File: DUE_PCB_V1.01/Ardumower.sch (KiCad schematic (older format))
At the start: 54 parts, among them J1 I2C0_1, J10 Bumper Left, J11 Bumper Right, J12 P_Left, J13 P_Right, J14 Sonar_R, J15 Sonar_C, J16 Sonar_L, J17 US1, J18 US2, J19 US3, J2 I2C0_2, J20 Button, J21 5V IN, J22 Remote, J23 PCB_2, J24 3.3V IN, J25 Ser0, J26 Ser1, J27 Ser2 (ESP32), J28 GPS_TX/GPS_RX, J3 I2C1_1, J5 9V IN, J6 Drop_Left, J7 Drop_Right, J8 Tilt, J9 Rain

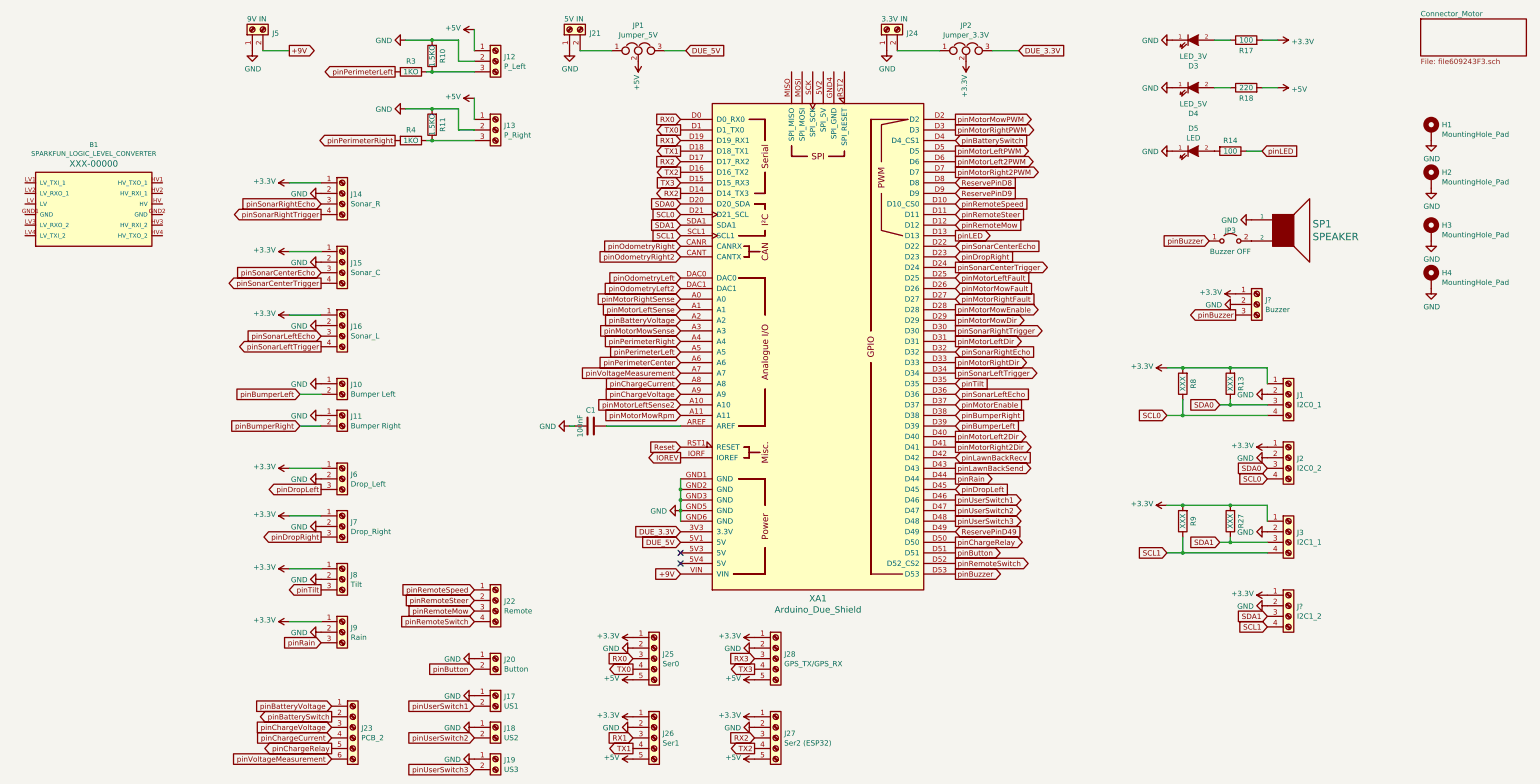
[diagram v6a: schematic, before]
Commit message: Add Reserve Pin Connectors
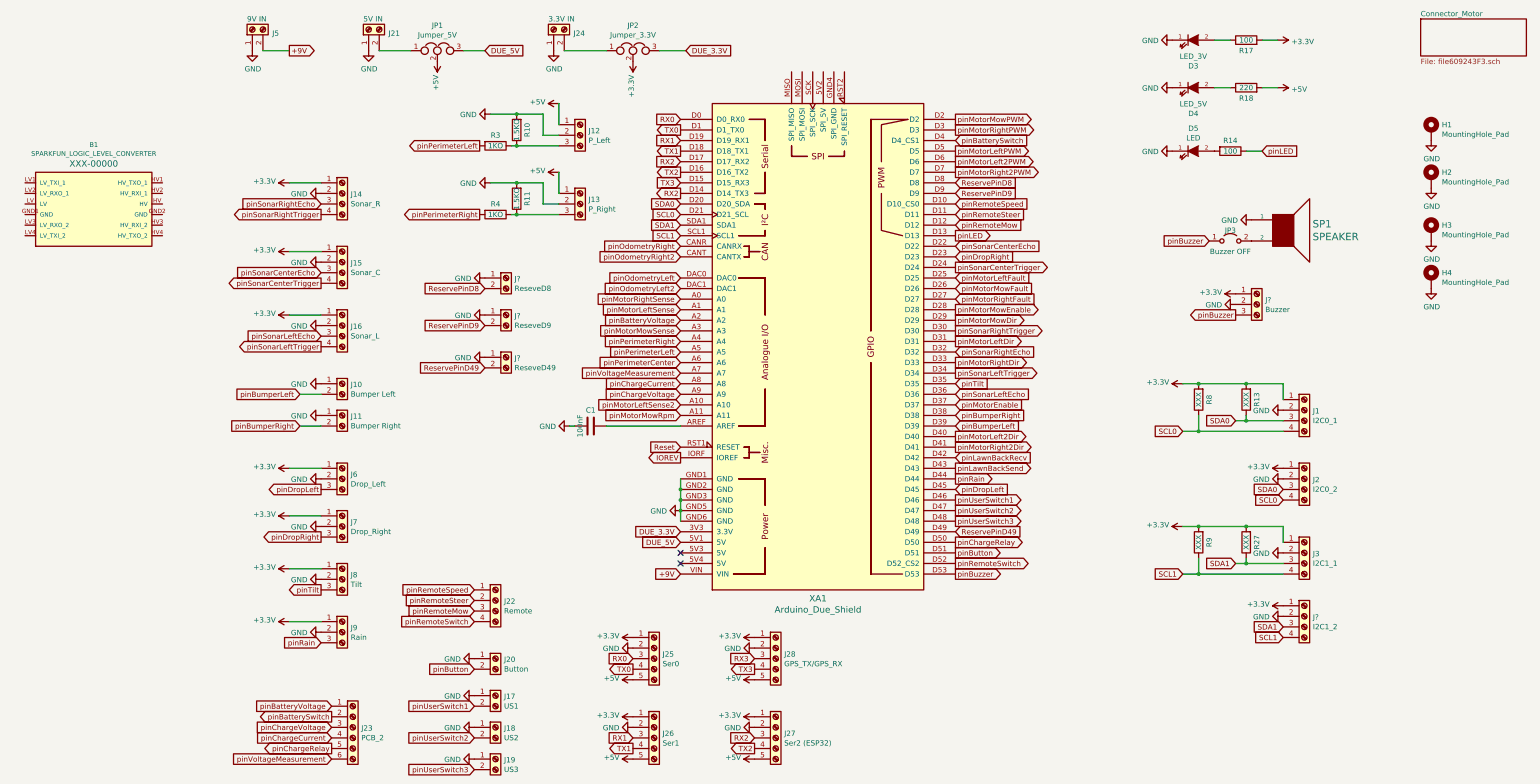
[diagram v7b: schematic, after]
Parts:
- added J?: ReseveD8, Zimprich:Pin_Header_KK110_1x02_3D, symbol Connector:Screw_Terminal_01x02
- added J?: ReseveD9, Zimprich:Pin_Header_KK110_1x02_3D, symbol Connector:Screw_Terminal_01x02
- added J?: ReseveD49, Zimprich:Pin_Header_KK110_1x02_3D, symbol Connector:Screw_Terminal_01x02
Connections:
- net GND: now also J?.1 (Pin_1), J?.1 (Pin_1), J?.1 (Pin_1)
- net ReservePinD49: now also J?.2 (Pin_2)
- net ReservePinD8: now also J?.2 (Pin_2)
- net ReservePinD9: now also J?.2 (Pin_2)
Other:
- moved on the sheet: J1, J12, J13, J2, J21, J24, J3, J?, JP1, JP2, R10, R11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

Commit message: Change Pin Header to JST
Change Pin Header to JST and sort them on the PCB
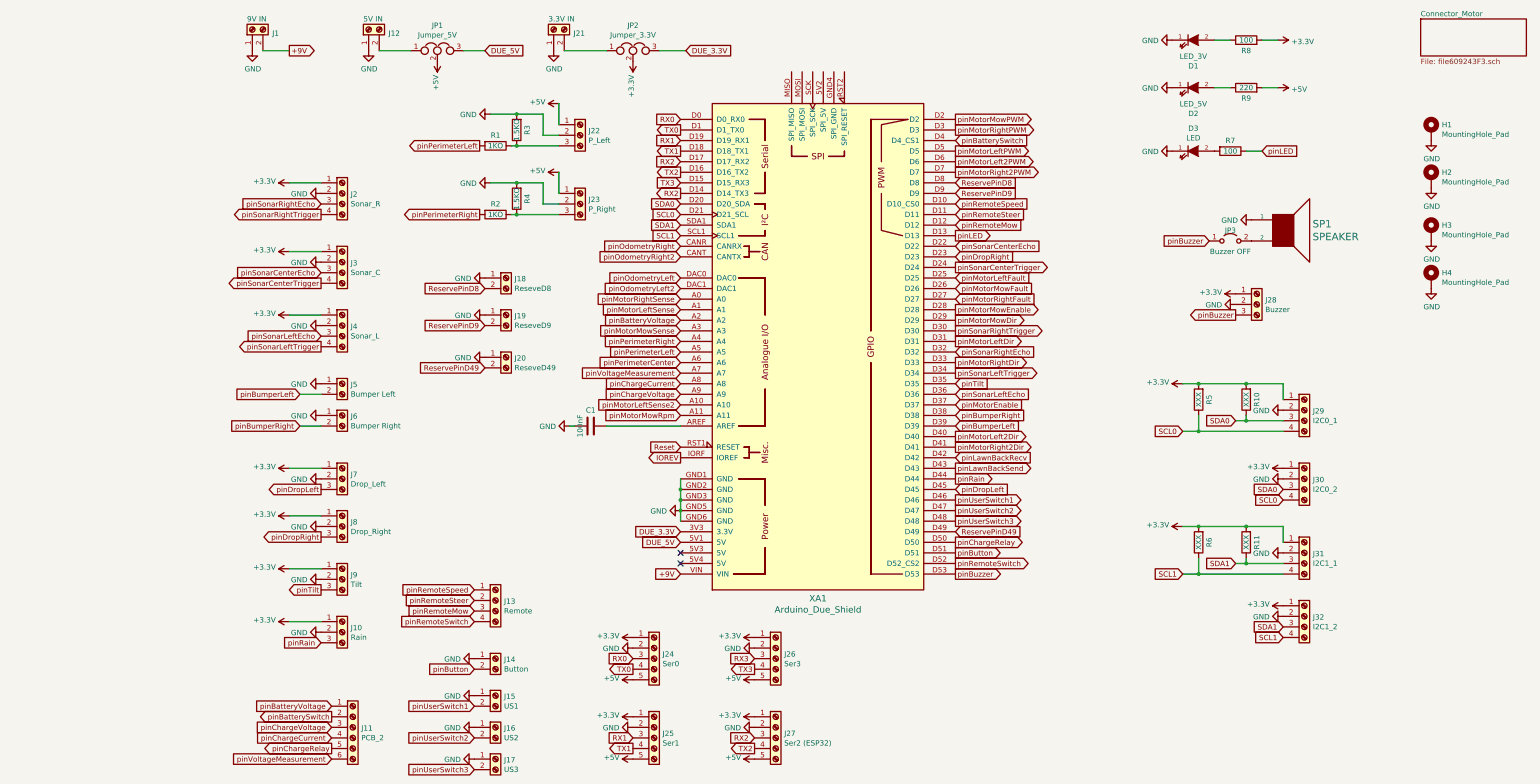
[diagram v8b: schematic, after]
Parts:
- removed B1: SPARKFUN_LOGIC_LEVEL_CONVERTER, Boards:SPARKFUN_LOGIC_LEVEL_CONVERTER, symbol SparkFun-Boards:SPARKFUN_LOGIC_LEVEL_CONVERTER
- J10: renamed from J9; footprint Connector_PinHeader_2.54mm:PinHeader_1x03_P2.54mm_Vertical -> Connector_JST:JST_XH_B3B-XH-A_1x03_P2.50mm_Vertical
- J11: renamed from J23; footprint Connector_PinHeader_2.54mm:PinHeader_1x06_P2.54mm_Vertical -> Connector_JST:JST_XH_B6B-XH-A_1x06_P2.50mm_Vertical
- J13: renamed from J22; footprint Connector_PinHeader_2.54mm:PinHeader_1x04_P2.54mm_Vertical -> Connector_JST:JST_XH_B4B-XH-A_1x04_P2.50mm_Vertical
- J14: renamed from J20; footprint Zimprich:Pin_Header_KK110_1x02_3D -> Connector_JST:JST_XH_B2B-XH-A_1x02_P2.50mm_Vertical
- J15: renamed from J17; footprint Zimprich:Pin_Header_KK110_1x02_3D -> Connector_JST:JST_XH_B2B-XH-A_1x02_P2.50mm_Vertical
- J16: renamed from J18; footprint Zimprich:Pin_Header_KK110_1x02_3D -> Connector_JST:JST_XH_B2B-XH-A_1x02_P2.50mm_Vertical
- J17: renamed from J19; footprint Zimprich:Pin_Header_KK110_1x02_3D -> Connector_JST:JST_XH_B2B-XH-A_1x02_P2.50mm_Vertical
- J18, J19, J20: renamed from J?; footprint Zimprich:Pin_Header_KK110_1x02_3D -> Connector_JST:JST_XH_B2B-XH-A_1x02_P2.50mm_Vertical
- J2: renamed from J14; footprint Connector_PinHeader_2.54mm:PinHeader_1x04_P2.54mm_Vertical -> Connector_JST:JST_XH_B4B-XH-A_1x04_P2.50mm_Vertical
- J22: renamed from J12; footprint Connector_PinHeader_2.54mm:PinHeader_1x03_P2.54mm_Vertical -> Connector_JST:JST_XH_B3B-XH-A_1x03_P2.50mm_Vertical
- J23: renamed from J13; footprint Connector_PinHeader_2.54mm:PinHeader_1x03_P2.54mm_Vertical -> Connector_JST:JST_XH_B3B-XH-A_1x03_P2.50mm_Vertical
- J24: renamed from J25; footprint Connector_PinHeader_2.54mm:PinHeader_1x05_P2.54mm_Vertical -> Connector_JST:JST_XH_B5B-XH-A_1x05_P2.50mm_Vertical
- J25: renamed from J26; footprint Connector_PinHeader_2.54mm:PinHeader_1x05_P2.54mm_Vertical -> Connector_JST:JST_XH_B5B-XH-A_1x05_P2.50mm_Vertical
- J26: renamed from J28; value GPS_TX/GPS_RX -> Ser3; footprint Connector_PinHeader_2.54mm:PinHeader_1x05_P2.54mm_Vertical -> Connector_JST:JST_XH_B5B-XH-A_1x05_P2.50mm_Vertical
- J27: footprint Connector_PinHeader_2.54mm:PinHeader_1x05_P2.54mm_Vertical -> Connector_JST:JST_XH_B5B-XH-A_1x05_P2.50mm_Vertical
- J28: renamed from J?; footprint Connector_PinHeader_2.54mm:PinHeader_1x03_P2.54mm_Vertical -> Connector_JST:JST_XH_B3B-XH-A_1x03_P2.50mm_Vertical
- J29: renamed from J1; footprint Connector_PinHeader_2.54mm:PinHeader_1x04_P2.54mm_Vertical -> Connector_JST:JST_XH_B4B-XH-A_1x04_P2.50mm_Vertical
- J3: renamed from J15; footprint Connector_PinHeader_2.54mm:PinHeader_1x04_P2.54mm_Vertical -> Connector_JST:JST_XH_B4B-XH-A_1x04_P2.50mm_Vertical
- J30: renamed from J2; footprint Connector_PinHeader_2.54mm:PinHeader_1x04_P2.54mm_Vertical -> Connector_JST:JST_XH_B4B-XH-A_1x04_P2.50mm_Vertical
- J31: renamed from J3; footprint Connector_PinHeader_2.54mm:PinHeader_1x04_P2.54mm_Vertical -> Connector_JST:JST_XH_B4B-XH-A_1x04_P2.50mm_Vertical
- J32: renamed from J?; footprint Connector_PinHeader_2.54mm:PinHeader_1x04_P2.54mm_Vertical -> Connector_JST:JST_XH_B4B-XH-A_1x04_P2.50mm_Vertical
- J4: renamed from J16; footprint Connector_PinHeader_2.54mm:PinHeader_1x04_P2.54mm_Vertical -> Connector_JST:JST_XH_B4B-XH-A_1x04_P2.50mm_Vertical
- J5: renamed from J10; footprint Connector_PinHeader_2.54mm:PinHeader_1x02_P2.54mm_Vertical -> Connector_JST:JST_XH_B2B-XH-A_1x02_P2.50mm_Vertical
- J6: renamed from J11; footprint Zimprich:Pin_Header_KK110_1x02_3D -> Connector_JST:JST_XH_B2B-XH-A_1x02_P2.50mm_Vertical
- J7: renamed from J6; footprint Connector_PinHeader_2.54mm:PinHeader_1x03_P2.54mm_Vertical -> Connector_JST:JST_XH_B3B-XH-A_1x03_P2.50mm_Vertical
- J8: renamed from J7; footprint Connector_PinHeader_2.54mm:PinHeader_1x03_P2.54mm_Vertical -> Connector_JST:JST_XH_B3B-XH-A_1x03_P2.50mm_Vertical
- J9: renamed from J8; footprint Connector_PinHeader_2.54mm:PinHeader_1x03_P2.54mm_Vertical -> Connector_JST:JST_XH_B3B-XH-A_1x03_P2.50mm_Vertical
- renumbered D3 to D1, D4 to D2, D5 to D3, J5 to J1, J21 to J12, J24 to J21, R3 to R1, R13 to R10, R27 to R11, R4 to R2, R10 to R3, R11 to R4, R8 to R5, R9 to R6, R14 to R7, R17 to R8, R18 to R9
